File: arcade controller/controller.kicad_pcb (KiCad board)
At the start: 2 copper layers, 203.5 x 152.2 mm, 21 parts, among them SW1 LEFT, SW10 SELECT, SW2 DOWN, SW3 RIGHT, SW4 UP, SW5 X, SW6 Y, SW7 A, SW8 B, SW9 START

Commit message: fixed con
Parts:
- ARCADE_PCB_CONN2: footprint Connector_Harwin:Harwin_Gecko-G125-FVX1205L0X_2x06_P1.25mm_Vertical -> Connector_PinHeader_2.54mm:PinHeader_2x06_P2.54mm_Vertical
- SW1: value LEFT -> SW_DIP_x01
- SW10: value SELECT -> SW_DIP_x01
- SW2: value DOWN -> SW_DIP_x01
- SW3: value RIGHT -> SW_DIP_x01
- SW4: value UP -> SW_DIP_x01
- SW5: value X -> SW_DIP_x01
- SW6: value Y -> SW_DIP_x01
- SW7: value A -> SW_DIP_x01
- SW8: value B -> SW_DIP_x01
- SW9: value START -> SW_DIP_x01
- moved ARCADE_PCB_CONN2 10.8 mm to (117.3, 25.0), turned to -90 degrees
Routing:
- net 3.3V: track 803.8 -> 715.4 mm, vias 6 -> 5
- net ARC3: track 123.7 -> 76.2 mm, vias 3 -> 1
- net ARC1: track 103.1 -> 57.6 mm
- net ARC7: track 155.0 -> 113.1 mm
- net ARC4: track 48.4 -> 11.0 mm
- net ARC2: track 131.3 -> 113.8 mm
- net ARC8: track 163.4 -> 146.5 mm, vias 3 -> 2
- net ARC10: track 176.3 -> 167.3 mm
- net ARC6: track 81.0 -> 74.7 mm
- net ARC9: track 140.1 -> 134.0 mm
- net ARC5: track 54.8 -> 49.4 mm

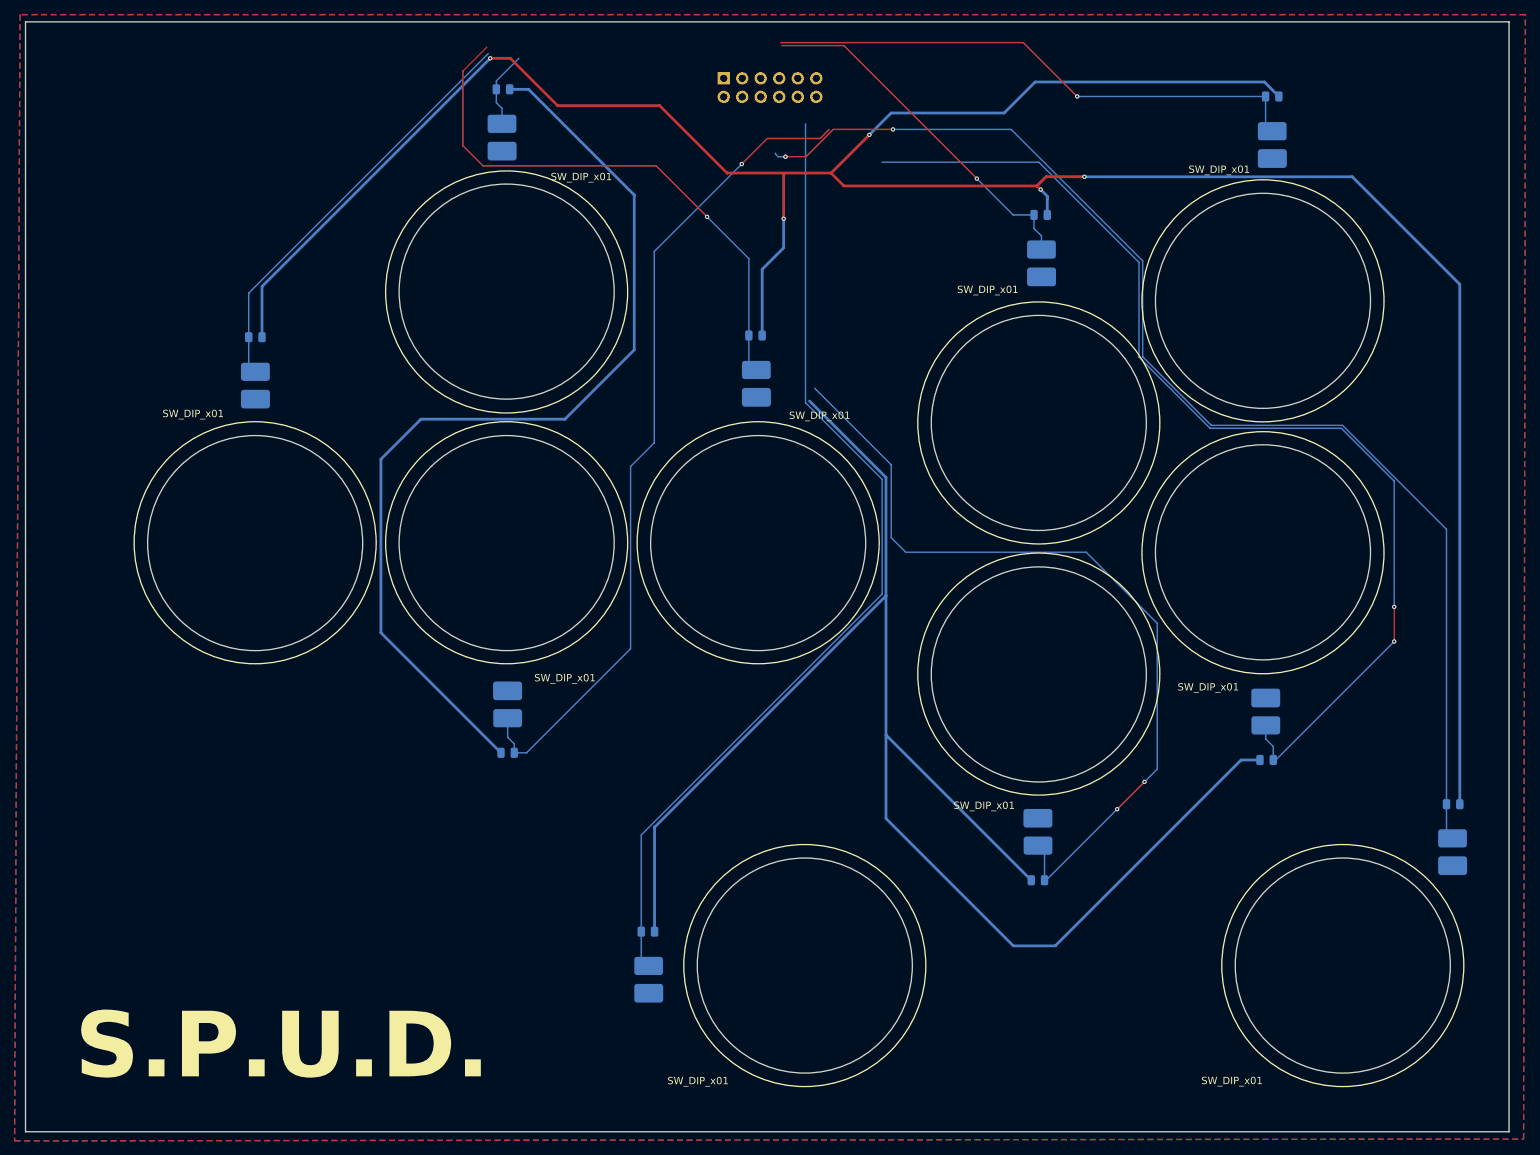
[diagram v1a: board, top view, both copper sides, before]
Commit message: wired new connector
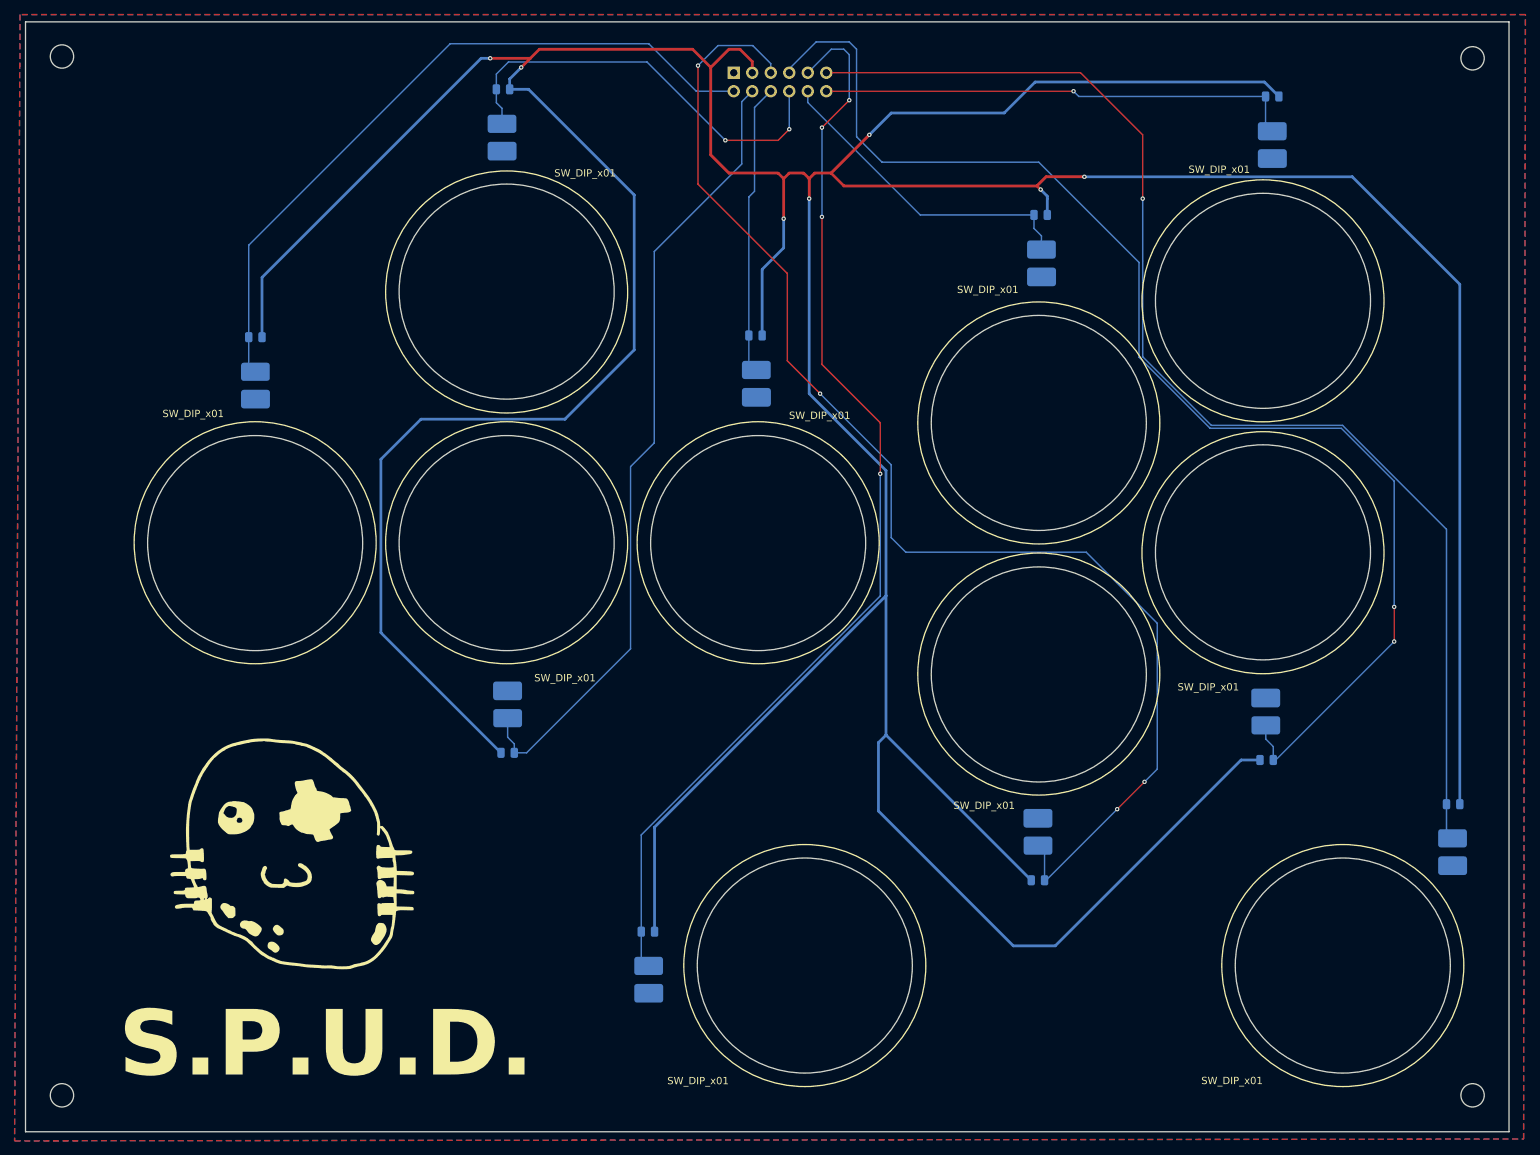
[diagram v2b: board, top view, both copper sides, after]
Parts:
- added G***: LOGO, spud real SMALL, F.Cu at (59.8, 132.5)
- added REF**: MountingHole_3.2mm_M3, MountingHole:MountingHole_3.2mm_M3, F.Cu at (26.5, 164.5)
- added REF**: MountingHole_3.2mm_M3, MountingHole:MountingHole_3.2mm_M3, F.Cu at (220.0, 22.2)
- added REF**: MountingHole_3.2mm_M3, MountingHole:MountingHole_3.2mm_M3, F.Cu at (220.0, 164.5)
- added REF**: MountingHole_3.2mm_M3, MountingHole:MountingHole_3.2mm_M3, F.Cu at (26.5, 22.0)
- ARCADE_PCB_CONN2: value Conn_02x06_Top_Bottom -> Conn_02x06_Odd_Even
- moved ARCADE_PCB_CONN2 1.58 mm to (118.7, 24.2)
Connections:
- ARCADE_PCB_CONN2 pad 1: ARC1 -> GND
- ARCADE_PCB_CONN2 pad 10: ARC10 -> ARC5
- ARCADE_PCB_CONN2 pad 11: 3.3V -> ARC10
- ARCADE_PCB_CONN2 pad 12: GND -> ARC6
- ARCADE_PCB_CONN2 pad 2: ARC2 -> ARC1
- ARCADE_PCB_CONN2 pad 3: ARC3 -> 3.3V
- ARCADE_PCB_CONN2 pad 4: ARC4 -> ARC2
- ARCADE_PCB_CONN2 pad 5: ARC5 -> ARC7
- ARCADE_PCB_CONN2 pad 6: ARC6 -> ARC3
- ARCADE_PCB_CONN2 pad 7: ARC7 -> ARC8
- ARCADE_PCB_CONN2 pad 8: ARC8 -> ARC4
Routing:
- net ARC7: track 113.1 -> 177.4 mm, vias 2 -> 4
- net 3.3V: track 715.4 -> 770.5 mm, vias 5 -> 7
- net ARC4: track 11.0 -> 58.7 mm, vias 0 -> 2
- net ARC1: track 57.6 -> 98.4 mm
- net ARC3: track 76.2 -> 39.9 mm, vias 1 -> 0
- net ARC8: track 146.5 -> 175.1 mm
- net ARC9: track 134.0 -> 151.2 mm, vias 0 -> 4
- net ARC6: track 74.7 -> 65.7 mm
- net ARC5: track 49.4 -> 44.1 mm, vias 1 -> 0
- net ARC10: track 167.3 -> 171.6 mm, vias 2 -> 1
- net ARC2: track 113.8 -> 110.4 mm, vias 1 -> 0
